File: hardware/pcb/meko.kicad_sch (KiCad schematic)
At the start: 0 parts

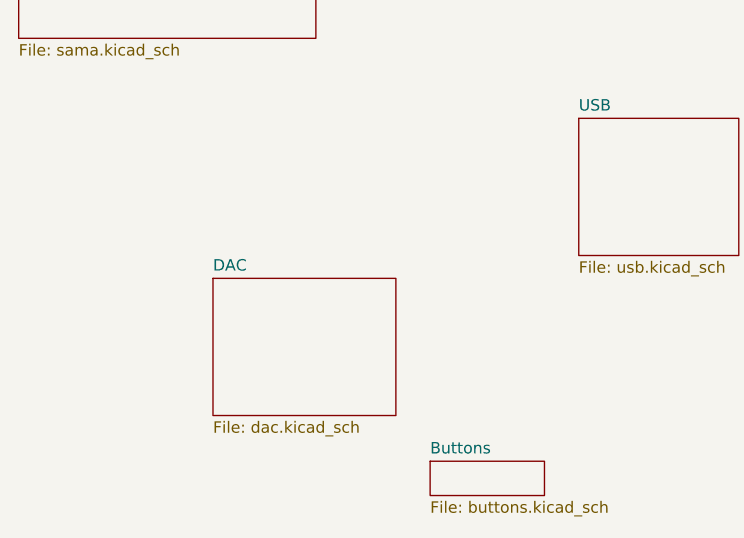
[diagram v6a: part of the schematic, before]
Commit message: bunch of small audio changes
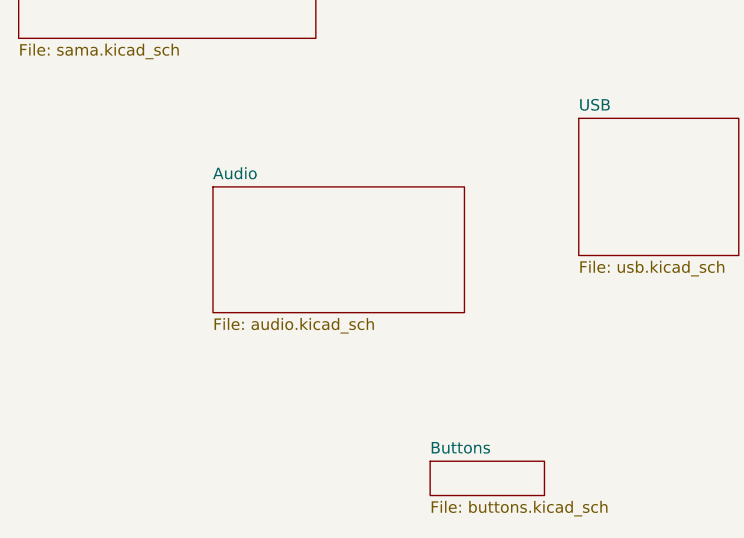
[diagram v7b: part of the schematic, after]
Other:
- removed sheet DAC
- added sheet Audio (audio.kicad_sch)
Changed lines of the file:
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@@
+	)
+	(sheet
+		(at 88.9 138.43)
+		(size 27.94 13.97)
+		(exclude_from_sim no)
+		(in_bom yes)
+		(on_board yes)
+		(dnp no)
+		(fields_autoplaced yes)
+		(stroke
+			(width 0.1524)
+			(type solid)
+		)
+		(fill
+			(color 0 0 0 0)
+		)
+		(property "Sheetname" "Audio"
+			(at 88.9 137.7184 0)
+			(show_name no)
+			(do_not_autoplace no)
+			(effects
+				(font
+					(size 1.27 1.27)
+				)
+				(justify left bottom)
+			)
+		)
+		(property "Sheetfile" "audio.kicad_sch"
+			(at 88.9 152.9846 0)
+			(show_name no)
+			(do_not_autoplace no)
+			(effects
+				(font
+					(size 1.27 1.27)
+				)
+				(justify left top)
+			)
+		)
+		(instances
+			(project "meko"
+				(path "/da54f10a-146b-4941-a9c7-55c7173bb101"
+					(page "7")
+				)
+			)
+		)
 	)
 	(sheet
@@
 				)
 			)
-		)
-	)
-	(sheet
-		(at 88.9 148.59)
-		(size 20.32 15.24)
-		(exclude_from_sim no)
-		(in_bom yes)
-		(on_board yes)
-		(dnp no)
-		(fields_autoplaced yes)
-		(stroke
-			(width 0.1524)
-			(type solid)
-		)
-		(fill
-			(color 0 0 0 0)
-		)
-		(property "Sheetname" "DAC"
-			(at 88.9 147.8784 0)
-			(show_name no)
-			(do_not_autoplace no)
-			(effects
-				(font
-					(size 1.27 1.27)
-				)
-				(justify left bottom)
-			)
-		)
-		(property "Sheetfile" "dac.kicad_sch"
-			(at 88.9 164.4146 0)
-			(show_name no)
-			(do_not_autoplace no)
-			(effects
-				(font
-					(size 1.27 1.27)
-				)
-				(justify left top)
-			)
-		)
-		(instances
-			(project "meko"
-				(path "/da54f10a-146b-4941-a9c7-55c7173bb101"
-					(page "7")
-				)
-			)

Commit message: moved stuff around
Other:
- sheet Audio ports: added DET_2.5mm, DET_3.5mm, {ASI}, {CODEC_GPIO}, {I2C}; removed none
- sheet Display ports: added {MIP}; removed none
- sheet Power ports: added CHG_~{INT}, FUEL_~{INT}, {I2C}, {PMIC_CTRL}, {USB_CC}; removed none
- sheet SD Cards ports: added BOOT{SDMMC}, EXT{SDMMC}; removed none
- sheet USB ports: added {USB_CC}, {USB}; removed none
- sheet Wireless ports: added BT{RF_CTRL}, WL{RF_CTRL}, {ASI}, {SDMMC}, {UART}; removed none
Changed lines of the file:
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@@
+			)
+		)
+		(pin "DET_2.5mm" output
+			(at 88.9 139.7 180)
+			(effects
+				(font
+					(size 1.27 1.27)
+				)
+				(justify left)
+			)
+		)
+		(pin "DET_3.5mm" output
+			(at 88.9 142.24 180)
+			(effects
+				(font
+					(size 1.27 1.27)
+				)
+				(justify left)
+			)
+		)
+		(pin "{ASI}" bidirectional
+			(at 88.9 144.78 180)
+			(effects
+				(font
+					(size 1.27 1.27)
+				)
+				(justify left)
+			)
+		)
+		(pin "{CODEC_GPIO}" bidirectional
+			(at 88.9 147.32 180)
+			(effects
+				(font
+					(size 1.27 1.27)
+				)
+				(justify left)
+			)
+		)
+		(pin "{I2C}" bidirectional
+			(at 88.9 149.86 180)
+			(effects
+				(font
+					(size 1.27 1.27)
+				)
+				(justify left)
 			)
 		)
@@
 			)
 		)
+		(pin "{MIP}" input
+			(at 196.85 148.59 180)
+			(effects
+				(font
+					(size 1.27 1.27)
+				)
+				(justify left)
+			)
+		)
 		(instances
 			(project "meko"
@@
 			)
 		)
+		(pin "{USB_CC}" input
+			(at 129.54 134.62 180)
+			(effects
+				(font
+					(size 1.27 1.27)
+				)
+				(justify left)
+			)
+		)
+		(pin "{USB}" input
+			(at 129.54 137.16 180)
+			(effects
+				(font
+					(size 1.27 1.27)
+				)
+				(justify left)
+			)
+		)
 		(instances
 			(project "meko"
@@
 			)
 		)
+		(pin "BOOT{SDMMC}" bidirectional
+			(at 149.86 160.02 180)
+			(effects
+				(font
+					(size 1.27 1.27)
+				)
+				(justify left)
+			)
+		)
+		(pin "EXT{SDMMC}" bidirectional
+			(at 149.86 162.56 180)
+			(effects
+				(font
+					(size 1.27 1.27)
+				)
+				(justify left)
+			)
+		)
 		(instances
 			(project "meko"
@@
 	(sheet
 		(at 173.99 53.34)
-		(size 12.7 24.13)
+		(size 15.24 24.13)
 		(exclude_from_sim no)
 		(in_bom yes)
@@
 			)
 		)
+		(pin "CHG_~{INT}" output
+			(at 173.99 55.88 180)
+			(effects
+				(font
+					(size 1.27 1.27)
+				)
+				(justify left)
+			)
+		)
+		(pin "FUEL_~{INT}" output
+			(at 173.99 58.42 180)
+			(effects
+				(font
+					(size 1.27 1.27)
+				)
+				(justify left)
+			)
+		)
+		(pin "{I2C}" bidirectional
+			(at 173.99 60.96 180)
+			(effects
+				(font
+					(size 1.27 1.27)
+				)
+				(justify left)
+			)
+		)
+		(pin "{PMIC_CTRL}" bidirectional
+			(at 173.99 63.5 180)
+			(effects
+				(font
+					(size 1.27 1.27)
+				)
+				(justify left)
+			)
+		)
+		(pin "{USB_CC}" bidirectional
+			(at 173.99 66.04 180)
+			(effects
+				(font
+					(size 1.27 1.27)
+				)
+				(justify left)
+			)
+		)
 		(instances
 			(project "meko"
@@
 			)
 		)
+		(pin "BT{RF_CTRL}" bidirectional
+			(at 170.18 99.06 180)
+			(effects
+				(font
+					(size 1.27 1.27)
+				)
+				(justify left)
+			)
+		)
+		(pin "WL{RF_CTRL}" bidirectional
+			(at 170.18 101.6 180)
+			(effects
+				(font
+					(size 1.27 1.27)
+				)
+				(justify left)
+			)
+		)
+		(pin "{ASI}" bidirectional
+			(at 170.18 104.14 180)
+			(effects
+				(font
+					(size 1.27 1.27)
+				)
+				(justify left)
+			)
+		)
+		(pin "{SDMMC}" bidirectional
+			(at 170.18 106.68 180)
+			(effects
+				(font
+					(size 1.27 1.27)
+				)
+				(justify left)
+			)
+		)
+		(pin "{UART}" bidirectional
+			(at 170.18 109.22 180)
+			(effects
+				(font
+					(size 1.27 1.27)
+				)
+				(justify left)
+			)
+		)
